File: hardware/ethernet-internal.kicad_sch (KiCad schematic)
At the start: 29 parts, among them J6 RJ45_Amphenol_RJMG1BD3B8K1ANR, U1 W5500, Y1 25MHz

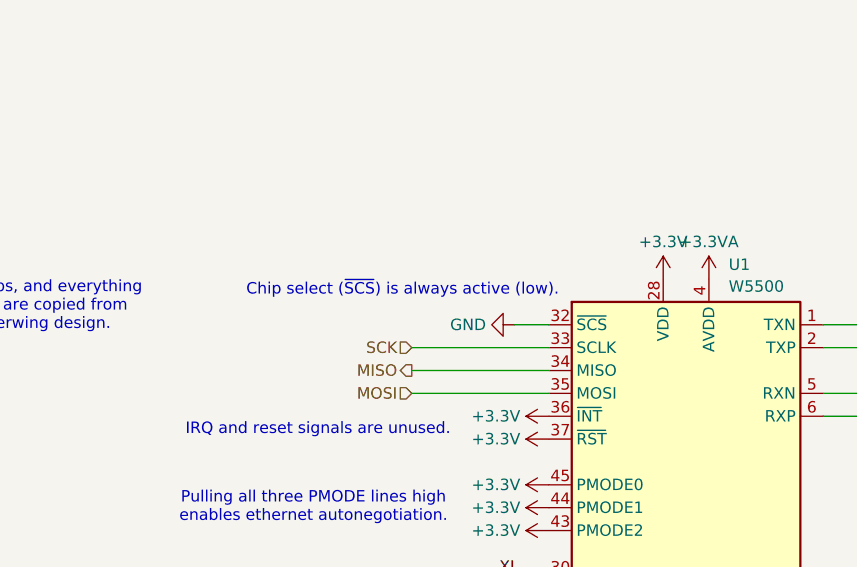
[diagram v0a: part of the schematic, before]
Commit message: Fix ethernet chip-select and register address decoder
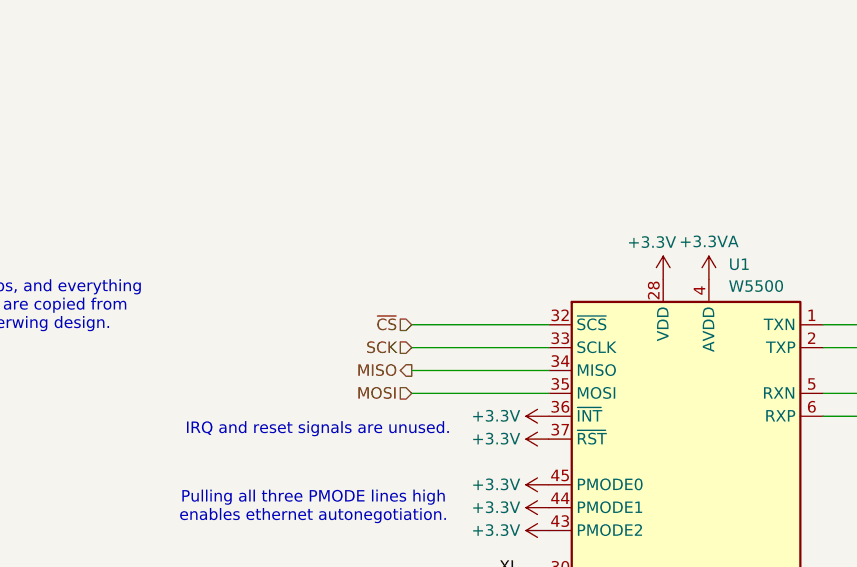
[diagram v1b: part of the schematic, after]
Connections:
- net GND: no longer U1.32 (~{SCS})
- new net ~{CS}: U1.32 (~{SCS})
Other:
- note removed: "Chip select (~{SCS}) is always active (low)."
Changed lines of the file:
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@@
 	(wire
 		(pts
-			(xy 100.33 91.44) (xy 104.14 91.44)
-		)
-		(stroke
-			(width 0)
-			(type default)
-		)
-	)
-	(wire
-		(pts
 			(xy 99.06 165.1) (xy 110.49 165.1)
 		)
@@
 	(wire
 		(pts
+			(xy 88.9 91.44) (xy 104.14 91.44)
+		)
+		(stroke
+			(width 0)
+			(type default)
+		)
+	)
+	(wire
+		(pts
 			(xy 149.86 120.65) (xy 152.4 120.65)
 		)
@@
 		)
 	)
-	(text "Chip select (~{SCS}) is always active (low)."
-		(exclude_from_sim no)
-		(at 87.884 87.63 0)
-		(effects
-			(font
-				(size 1.27 1.27)
-			)
-		)
-	)
 	(text "IRQ and reset signals are unused."
 		(exclude_from_sim no)
@@
 		)
 	)
+	(hierarchical_label "~{CS}"
+		(shape input)
+		(at 88.9 91.44 180)
+		(fields_autoplaced yes)
+		(effects
+			(font
+				(size 1.27 1.27)
+			)
+			(justify right)
+		)
+	)
 	(hierarchical_label "MISO"
 		(shape output)
@@
 		(on_board yes)
 		(dnp no)
-		(fields_autoplaced yes)
 		(property "Reference" "#PWR091"
 			(at 116.84 90.17 0)
@@
 		)
 		(property "Value" "+3.3V"
-			(at 116.84 82.2269 0)
+			(at 115.57 82.296 0)
 			(effects
 				(font
@@
 					(unit 1)
 				)
-			)
-		)
-	)
-	(symbol
-		(lib_id "power:GND")
-		(at 100.33 91.44 270)
-		(unit 1)
-		(exclude_from_sim no)
-		(in_bom yes)
-		(on_board yes)
-		(dnp no)
-		(fields_autoplaced yes)
-		(property "Reference" "#PWR0117"
-			(at 93.98 91.44 0)
-			(effects
-				(font
-					(size 1.27 1.27)
-				)
-				(hide yes)
-			)
-		)
-		(property "Value" "GND"
-			(at 97.1551 91.44 90)
-			(effects
-				(font
-					(size 1.27 1.27)
-				)
-				(justify right)
-			)
-		)
-		(property "Footprint" ""
-			(at 100.33 91.44 0)
-			(effects
-				(font
-					(size 1.27 1.27)
-				)
-				(hide yes)
-			)
-		)
-		(property "Datasheet" ""
-			(at 100.33 91.44 0)
-			(effects
-				(font
-					(size 1.27 1.27)
-				)
-				(hide yes)
-			)
-		)
-		(property "Description" "Power symbol creates a global label with name \"GND\" , ground"
-			(at 100.33 91.44 0)
-			(effects
-				(font
-					(size 1.27 1.27)
-				)
-				(hide yes)
-			)
-		)
-		(pin "1"
-		)
-		(instances
-			(project ""
-				(path "/eb0e957f-b2ea-4261-97c1-e28148a3f6e1/615a7c3e-7c73-493c-85cc-9308526429fc"
-					(reference "#PWR0117")
-					(unit 1)
-				)

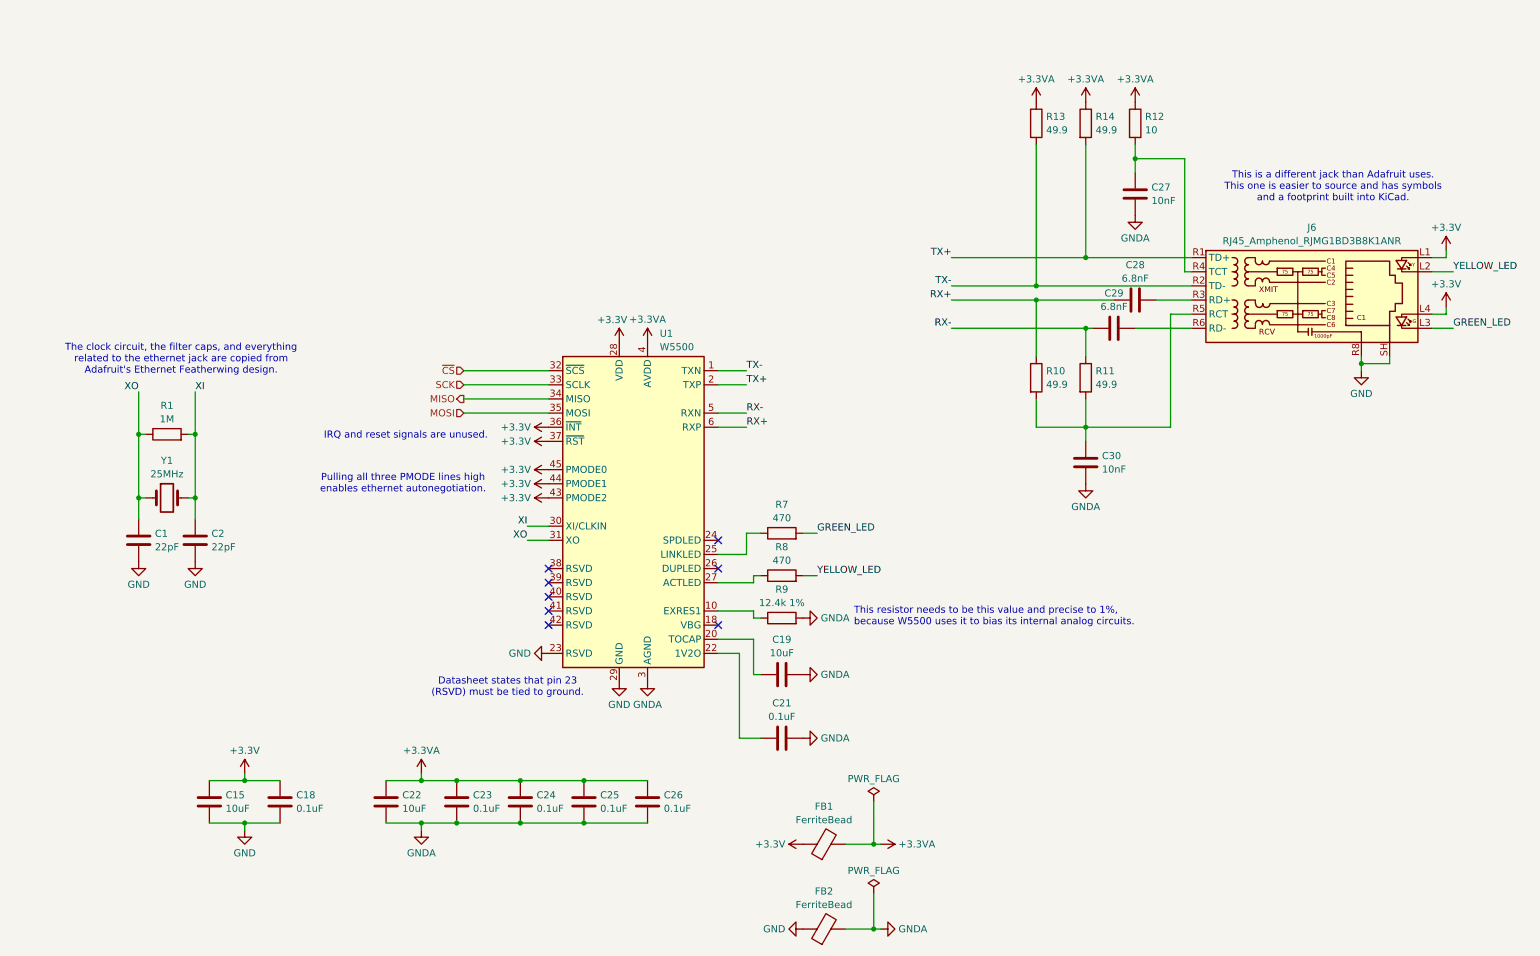
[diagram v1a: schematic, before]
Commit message: Revise microcontroller board based on latest cart board improvements
 - Update comments
 - Segregate the Ethernet module's power supply so it can be
   disconnected if something goes wrong in a prototype
 - Update board setup to match latest cart board
 - Remove unnecessary level-shifter
 - Fix address decoder to non-latching version
 - Fix address decoder output assignment
 - Consolidate buffer ICs in register file
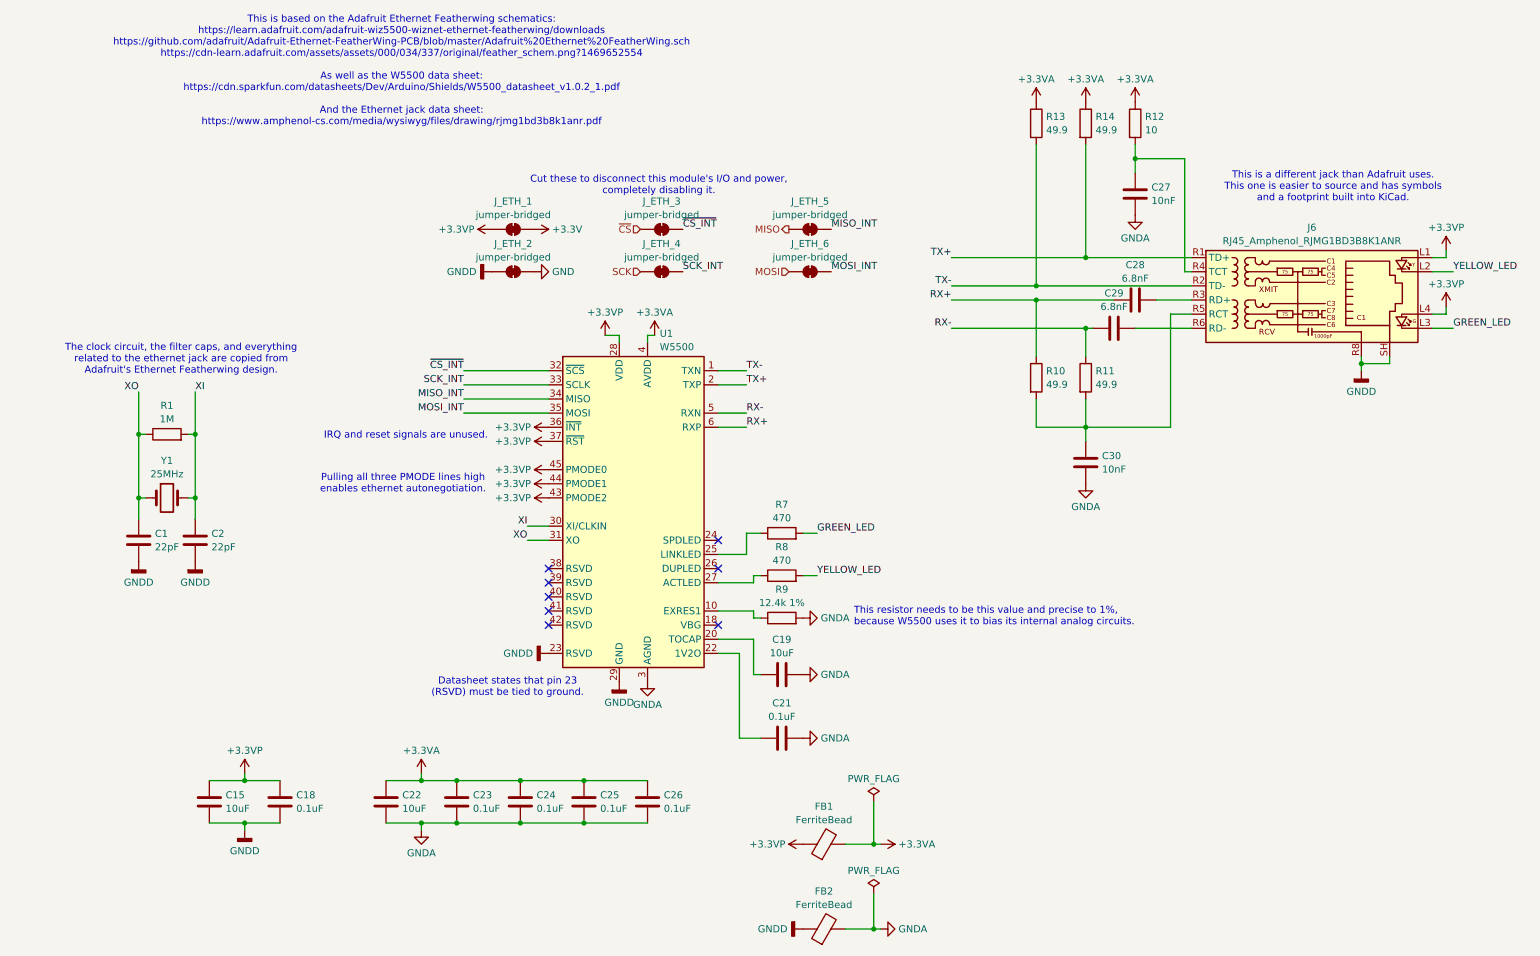
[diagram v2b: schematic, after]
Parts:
- added J_ETH_1, J_ETH_2, J_ETH_3, J_ETH_4, J_ETH_5, J_ETH_6: jumper-bridged, Jumper:SolderJumper-2_P1.3mm_Bridged_RoundedPad1.0x1.5mm, symbol Jumper:SolderJumper_2_Bridged
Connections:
- net +3.3V: now also J_ETH_1.2 (B); no longer C15.1, C18.1, FB1.1, J6.L1, J6.L4, U1.28 (VDD), U1.36 (~{INT}), U1.37 (~{RST}), U1.43 (PMODE2), U1.44 (PMODE1), U1.45 (PMODE0)
- net GND: now also J_ETH_2.2 (B); no longer C1.2, C15.2, C18.2, C2.2, FB2.1, J6.R8, J6.SH, U1.23 (RSVD), U1.29 (GND)
- net MISO: now also J_ETH_5.1 (A); no longer U1.34 (MISO)
- net MOSI: now also J_ETH_6.1 (A); no longer U1.35 (MOSI)
- net SCK: now also J_ETH_4.1 (A); no longer U1.33 (SCLK)
- net ~{CS}: now also J_ETH_3.1 (A); no longer U1.32 (~{SCS})
- new net +3.3VP: C15.1, C18.1, FB1.1, J6.L1, J6.L4, J_ETH_1.1 (A), U1.28 (VDD), U1.36 (~{INT}), U1.37 (~{RST}), U1.43 (PMODE2), U1.44 (PMODE1), U1.45 (PMODE0)
- new net GNDD: C1.2, C15.2, C18.2, C2.2, FB2.1, J6.R8, J6.SH, J_ETH_2.1 (A), U1.23 (RSVD), U1.29 (GND)
- new net MISO_INT: J_ETH_5.2 (B), U1.34 (MISO)
- new net MOSI_INT: J_ETH_6.2 (B), U1.35 (MOSI)
- new net SCK_INT: J_ETH_4.2 (B), U1.33 (SCLK)
- new net ~{CS_INT}: J_ETH_3.2 (B), U1.32 (~{SCS})
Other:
- note added: "Cut these to disconnect this module's I/O and power, completely disabling it."
- note added: "This is based on the Adafruit Ethernet Featherwing schematics: https://learn.adafruit.com/adafruit-wiz5500-wiznet-ethernet-featherwing/downloads https://github.com/adafruit/Adafruit-Ethernet-FeatherWing-PCB/blob/master/Adafruit%20Ethernet%20FeatherWing.sch https://cdn-learn.adafruit.com/assets/assets/000/034/337/original/feather_schem.png?1469652554 As well as the W5500 data sheet: https://cdn.sp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"
